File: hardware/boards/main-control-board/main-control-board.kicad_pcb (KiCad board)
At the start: 2 copper layers, 90.5 x 50 mm, 40 parts, among them J1 Conn_01x02_Pin_Speaker, J2 Conn_OLED, J3 Conn_extension, J4 Conn_02x06_Odd_Even, J7 Conn_ESP32, J8 Conn_ESP32, U1 PCA9685PW,118, U2 HX PZ2.54-3X5P ZZ, U3 MAX98357AETE+T, U4 TPS259571DSGR

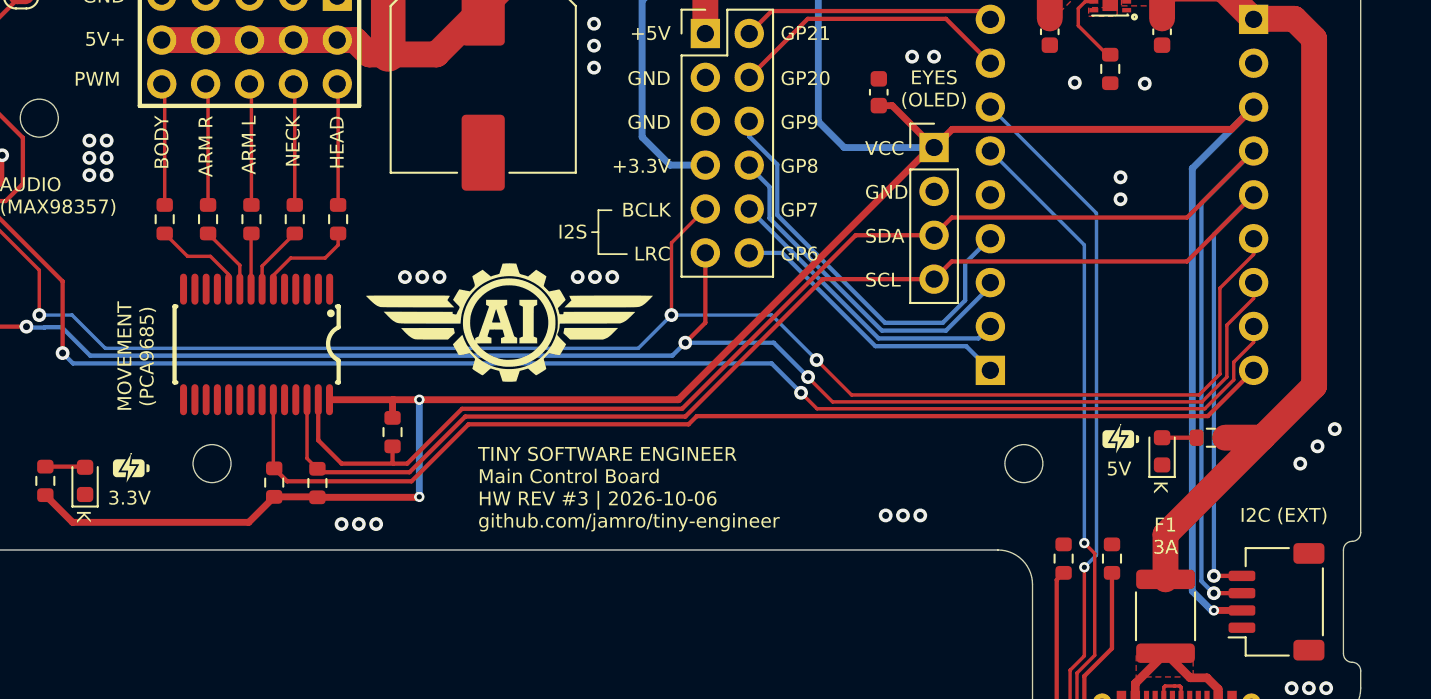
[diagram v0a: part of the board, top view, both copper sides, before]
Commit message: add ESP antenna keepout
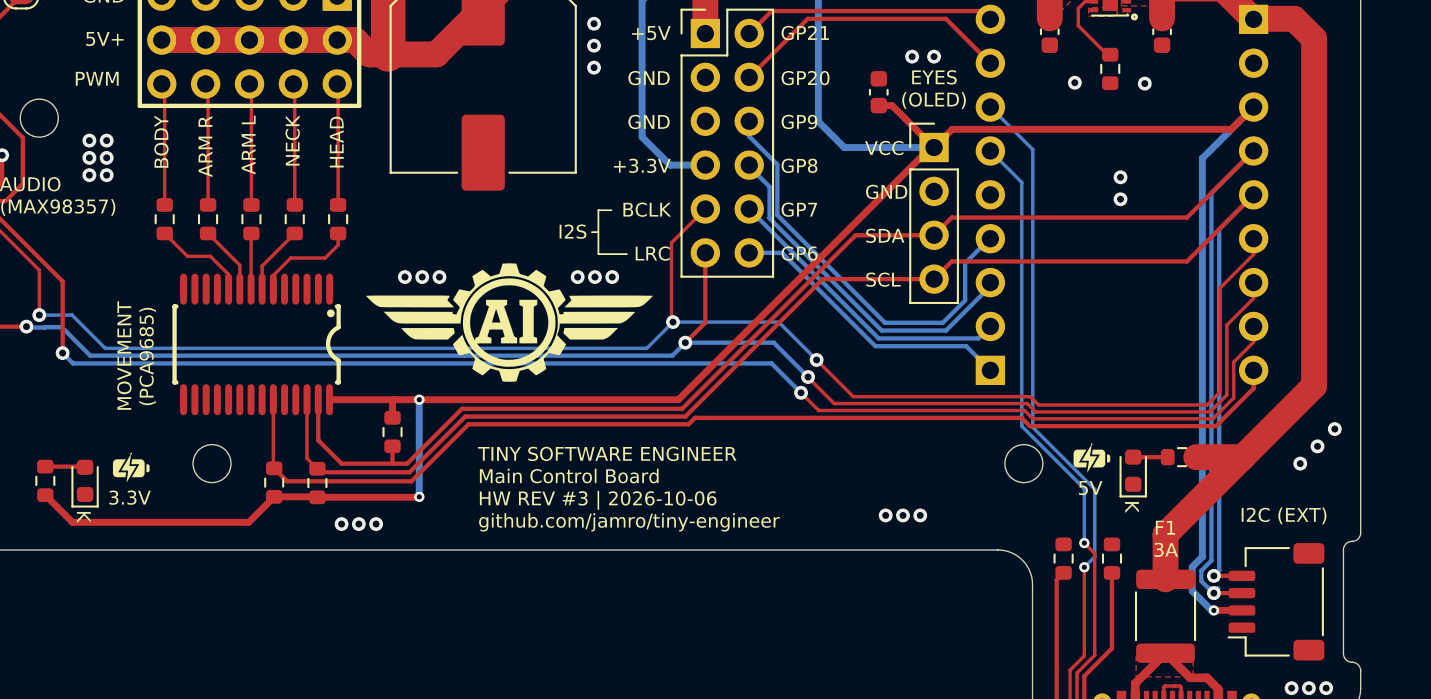
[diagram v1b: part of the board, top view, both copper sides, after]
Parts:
- moved D1 2.01 mm to (189.3, 115.4)
- moved R11 2.01 mm to (192.2, 114.6)
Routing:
- net /I2S_BCLK: track 95.7 -> 96.9 mm
- net /I2S_LRC: track 93.5 -> 94.6 mm
- net /I2S_DIN: track 83.9 -> 85.0 mm
- net /ESP32/GP5: track 63.7 -> 64.7 mm
- net /I2C_SDA: track 93.5 -> 94.0 mm
- net +5V: track 48.8 -> 49.3 mm

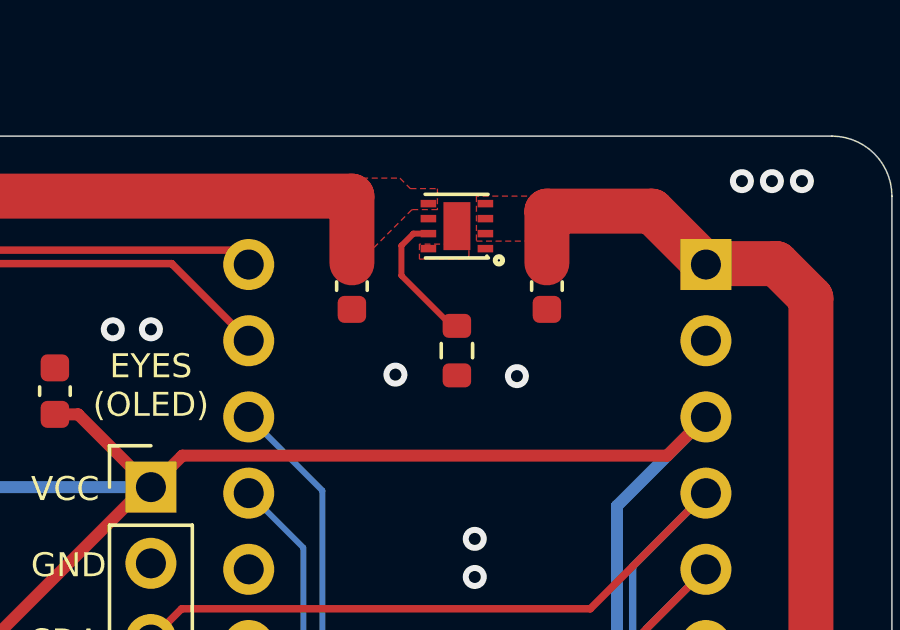
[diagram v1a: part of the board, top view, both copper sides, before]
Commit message: add 100nF to U4 dVdt
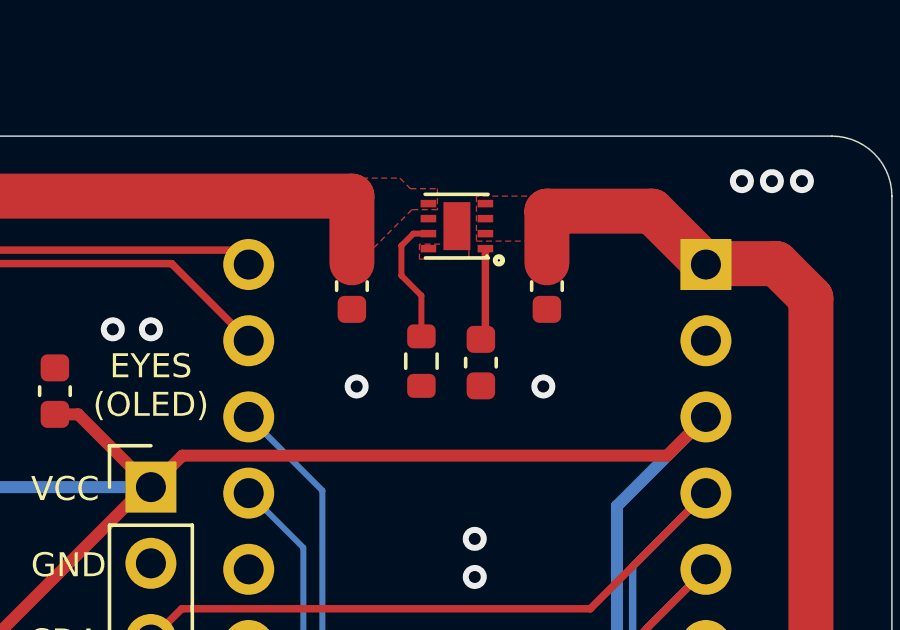
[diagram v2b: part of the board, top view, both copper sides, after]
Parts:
- added C6: 100nF, Capacitor_SMD:C_0603_1608Metric, F.Cu at (188.8, 92.5)
- moved R14 1.23 mm to (186.8, 92.5)
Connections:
- U4 pad 1: unconnected-(U4-dVdt-Pad1) -> Net-(U4-dVdt)
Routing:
- net Net-(U4-dVdt): track 0.00 -> 3.09 mm
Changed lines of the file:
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@@
 	(footprint "Resistor_SMD:R_0603_1608Metric"
 		(layer "F.Cu")
-		(at 188 92.15 -90)
+		(at 186.817 92.5 -90)
 		(descr "Resistor SMD 0603 (1608 Metric), square (rectangular) end terminal, IPC-7351 nominal, (Body size source: IPC-SM-782 page 72, https://www.pcb-3d.com/wordpress/wp-content/uploads/ipc-sm-782a_amendment_1_and_2.pdf)")
 		(tags "resistor")
@@
 			(size 0.521 0.25)
 			(layers "F.Cu" "F.Mask" "F.Paste")
-			(net "unconnected-(U4-dVdt-Pad1)")
+			(net "Net-(U4-dVdt)")
 			(pinfunction "dVdt_1")
-			(pintype "passive+no_connect")
+			(pintype "passive")
 		)
 		(pad "2" smd rect
@@
 		)
 	)
+	(footprint "Capacitor_SMD:C_0603_1608Metric"
+		(layer "F.Cu")
+		(at 188.8 92.55 -90)
+		(descr "Capacitor SMD 0603 (1608 Metric), square (rectangular) end terminal, IPC-7351 nominal, (Body size source: IPC-SM-782 page 76, https://www.pcb-3d.com/wordpress/wp-content/uploads/ipc-sm-782a_amendment_1_and_2.pdf)")
+		(tags "capacitor")
+		(property "Reference" "C6"
+			(at 0 -1.43 90)
+			(layer "F.SilkS")
+			(hide yes)
+			(effects
+				(font
+					(size 1 1)
+					(thickness 0.15)
+				)
+			)
+		)
+		(property "Value" "100nF"
+			(at 0 1.43 90)
+			(layer "F.Fab")
+			(effects
+				(font
+					(size 1 1)
+					(thickness 0.15)
+				)
+			)
+		)
+		(property "Datasheet" ""
+			(at 0 0 90)
+			(layer "F.Fab")
+			(hide yes)
+			(effects
+				(font
+					(size 1.27 1.27)
+				)
+			)
+		)
+		(property "Description" "Unpolarized capacitor"
+			(at 0 0 90)
+			(layer "F.Fab")
+			(hide yes)
+			(effects
+				(font
+					(size 1.27 1.27)
+				)
+			)
+		)
+		(property "KiLib_Generator" ""
+			(at 0 0 90)
+			(layer "F.SilkS")
+			(hide yes)
+			(effects
+				(font
+					(size 1 1)
+					(thickness 0.15)
+				)
+			)
+		)
+		(property "LCSC Part #" "C14663"
+			(at 0 0 270)
+			(unlocked yes)
+			(layer "F.Fab")
+			(hide yes)
+			(effects
+				(font
+					(size 1 1)
+					(thickness 0.15)
+				)
+			)
+		)
+		(property "MPN" "CC0603KRX7R9BB104"
+			(at 0 0 270)
+			(unlocked yes)
+			(layer "F.Fab")
+			(hide yes)
+			(effects
+				(font
+					(size 1 1)
+					(thickness 0.15)
+				)
+			)
+		)
+		(property "Manufacturer" "YAGEO"
+			(at 0 0 270)
+			(unlocked yes)
+			(layer "F.Fab")
+			(hide yes)
+			(effects
+				(font
+					(size 1 1)
+					(thickness 0.15)
+				)
+			)
+		)
+		(property ki_fp_filters "C_*")
+		(sheetname "/PCA/")
+		(sheetfile "main-control-board-pca.kicad_sch")
+		(units
+			(unit
+				(name "A")
+				(pins "1" "2")
+			)
+		)
+		(attr smd)
+		(duplicate_pad_numbers_are_jumpers no)
+		(fp_line
+			(start -0.14058 0.51)
+			(end 0.14058 0.51)
+			(stroke
+				(width 0.12)
+				(type solid)
+			)
+			(layer "F.SilkS")
+		)
+		(fp_line
+			(start -0.14058 -0.51)
+			(end 0.14058 -0.51)
+			(stroke
+				(width 0.12)
+				(type solid)
+			)
+			(layer "F.SilkS")
+		)
+		(fp_rect
+			(start -1.48 -0.73)
+			(end 1.48 0.73)
+			(stroke
+				(width 0.05)
+				(type solid)
+			)
+			(fill no)
+			(layer "F.CrtYd")
+		)
+		(fp_rect
+			(start -0.8 -0.4)
+			(end 0.8 0.4)
+			(stroke
+				(width 0.1)
+				(type solid)
+			)
+			(fill no)
+			(layer "F.Fab")
+		)
+		(fp_text user "${REFERENCE}"
+			(at 0 0 90)
+			(layer "F.Fab")
+			(effects
+				(font
+					(size 0.4 0.4)
+					(thickness 0.06)
+				)
+			)
+		)
+		(pad "1" smd roundrect
+			(at -0.775 0 270)
+			(size 0.9 0.95)
+			(layers "F.Cu" "F.Mask" "F.Paste")
+			(roundrect_rratio 0.25)
+			(net "Net-(U4-dVdt)")
+			(pintype "passive")
+		)
+		(pad "2" smd roundrect
+			(at 0.775 0 270)
+			(size 0.9 0.95)
+			(layers "F.Cu" "F.Mask" "F.Paste")
+			(roundrect_rratio 0.25)
+			(net "GND")
+			(pintype "passive")
+		)
+		(embedded_fonts no)
+		(model "${KICAD10_3DMODEL_DIR}/Capacitor_SMD.3dshapes/C_0603_1608Metric.step"
+			(offset
+				(xyz 0 0 0)
+			)
+			(scale
+				(xyz 1 1 1)
+			)
+			(rotate
+				(xyz 0 0 0)
+			)
+		)
+	)
 	(footprint "Resistor_SMD:R_0603_1608Metric"
 		(layer "F.Cu")
@@
 	)
 	(via
-		(at 185.95 92.95)
-		(size 0.8)
-		(drill 0.4)
-		(layers "F.Cu" "B.Cu")
-		(free yes)
-		(net "GND")
-	)
-	(via
 		(at 129.9 96.3)
 		(size 0.8)
@@
 	)
 	(via
+		(at 184.658 93.345)
+		(size 0.8)
+		(drill 0.4)
+		(layers "F.Cu" "B.Cu")
+		(free yes)
+		(net "GND")
+	)
+	(via
 		(at 198.5 86.5)
 		(size 0.8)
@@
 	)
 	(via
-		(at 200.5 128)
+		(at 190.881 93.345)
 		(size 0.8)
 		(drill 0.4)
@@
 	)
 	(via
-		(at 190 93)
+		(at 200.5 128)
 		(size 0.8)
 		(drill 0.4)
@@
 	)
 	(segment
-		(start 187.825 91.325)
-		(end 186.15 89.65)
+		(start 186.55 88.25)
+		(end 186.15 88.65)
 		(width 0.2)
 		(layer "F.Cu")
@@
 	)
 	(segment
-		(start 186.55 88.25)
-		(end 187.05 88.25)
+		(start 187.05 88.25)
+		(end 186.55 88.25)
 		(width 0.2)
 		(layer "F.Cu")
@@
 	)
 	(segment
-		(start 186.15 88.65)
-		(end 186.55 88.25)
+		(start 186.817 90.317)
+		(end 186.817 91.675)
 		(width 0.2)
 		(layer "F.Cu")
@@
 	)
 	(segment
-		(start 188 91.325)
-		(end 187.825 91.325)
+		(start 186.15 89.65)
+		(end 186.817 90.317)
 		(width 0.2)
 		(layer "F.Cu")
@@
 	)
 	(segment
-		(start 186.15 89.65)
-		(end 186.15 88.65)
+		(start 186.15 88.65)
+		(end 186.15 89.65)
 		(width 0.2)
 		(layer "F.Cu")
@@
 		(net "Net-(D2-A)")
 	)
+	(segment
+		(start 188.95 88.75)
+		(end 188.95 91.625)
+		(width 0.25)
+		(layer "F.Cu")
+		(net "Net-(U4-dVdt)")
+	)
+	(segment
+		(start 188.95 91.625)
+		(end 188.8 91.775)
+		(width 0.25)
+		(layer "F.Cu")
+		(net "Net-(U4-dVdt)")
+	)
 	(zone

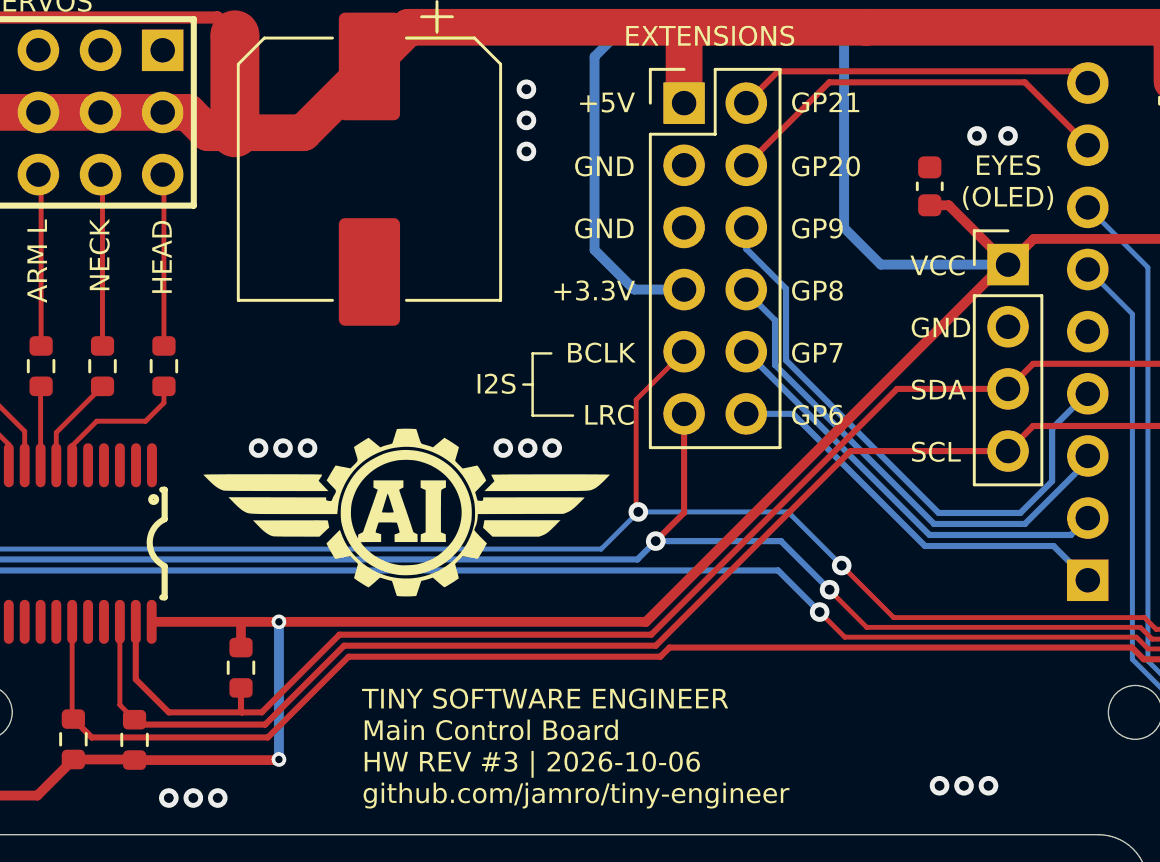
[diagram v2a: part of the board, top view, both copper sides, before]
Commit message: add capacitor next to pin 28 of PCA
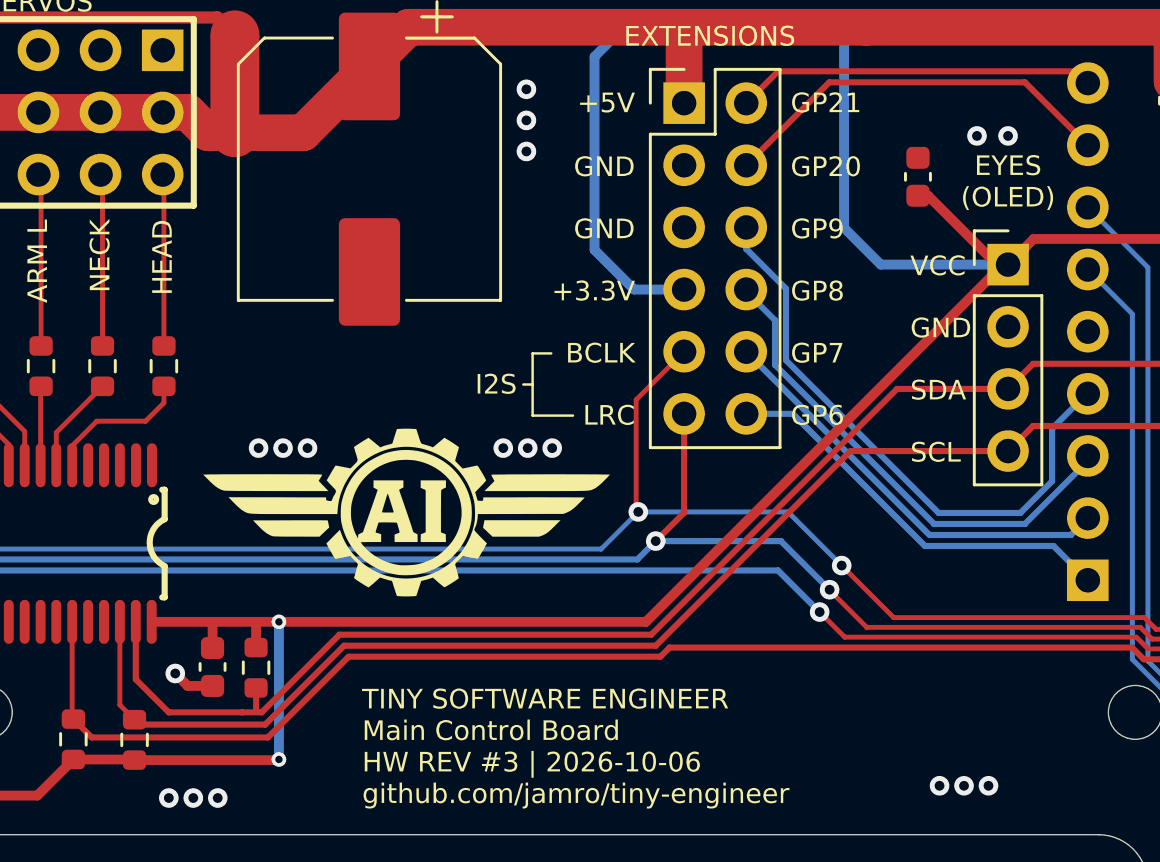
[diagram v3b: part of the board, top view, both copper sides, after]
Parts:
- added C7: 100nF, Capacitor_SMD:C_0603_1608Metric, F.Cu at (174.1, 93.1)
- moved C1 35.3 mm to (145.3, 113.1), turned to 90 degrees
- moved R5 0.62 mm to (147.1, 113.2)
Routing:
- net GND: track 9.89 -> 11.6 mm, vias 44 -> 45
- net +3.3V: track 165.5 -> 167.2 mm

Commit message: update silkscreen text on main control board: change label from "GP9" to "BOOT" and modify "GP8" to "GP8*"
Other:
- board text added: "BOOT"
- board text added: "GP8*"
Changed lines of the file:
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@@
 		)
 	)
-	(gr_text "GP9"
+	(gr_text "BOOT"
 		(at 168.91 95.25 0)
 		(layer "F.SilkS")
@@
 		)
 	)
-	(gr_text "GP8"
+	(gr_text "GP8*"
 		(at 168.91 97.79 0)
 		(layer "F.SilkS")
